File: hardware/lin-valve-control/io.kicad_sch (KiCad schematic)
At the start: 23 parts

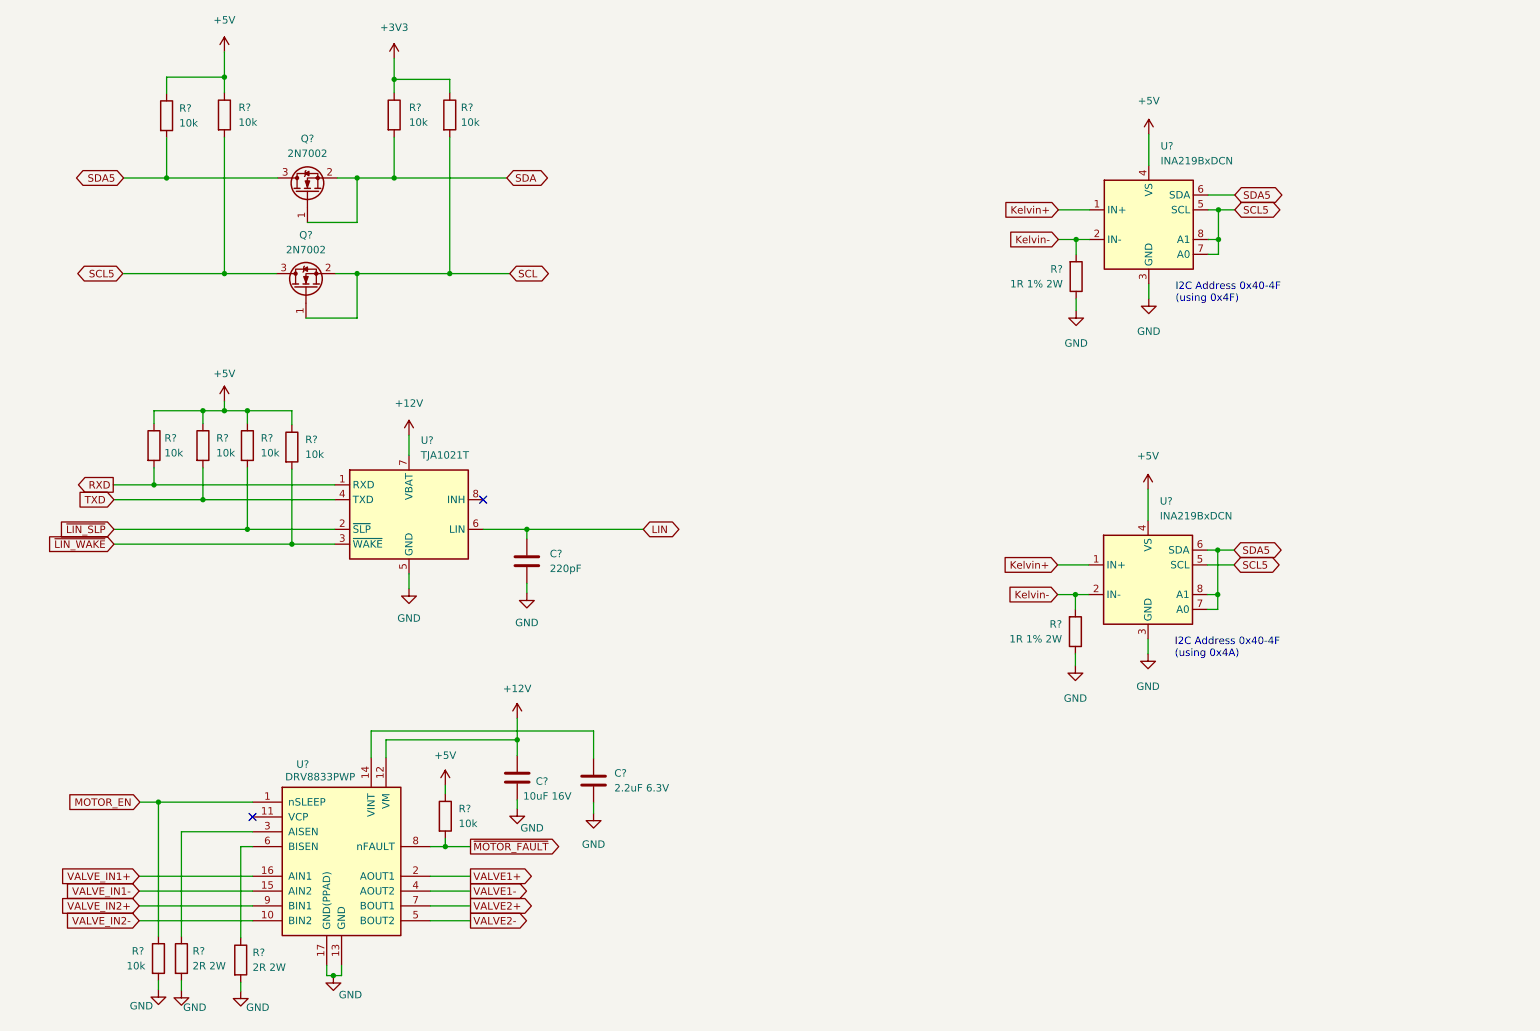
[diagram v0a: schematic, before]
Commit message: Update lin-master firmware and valve control board
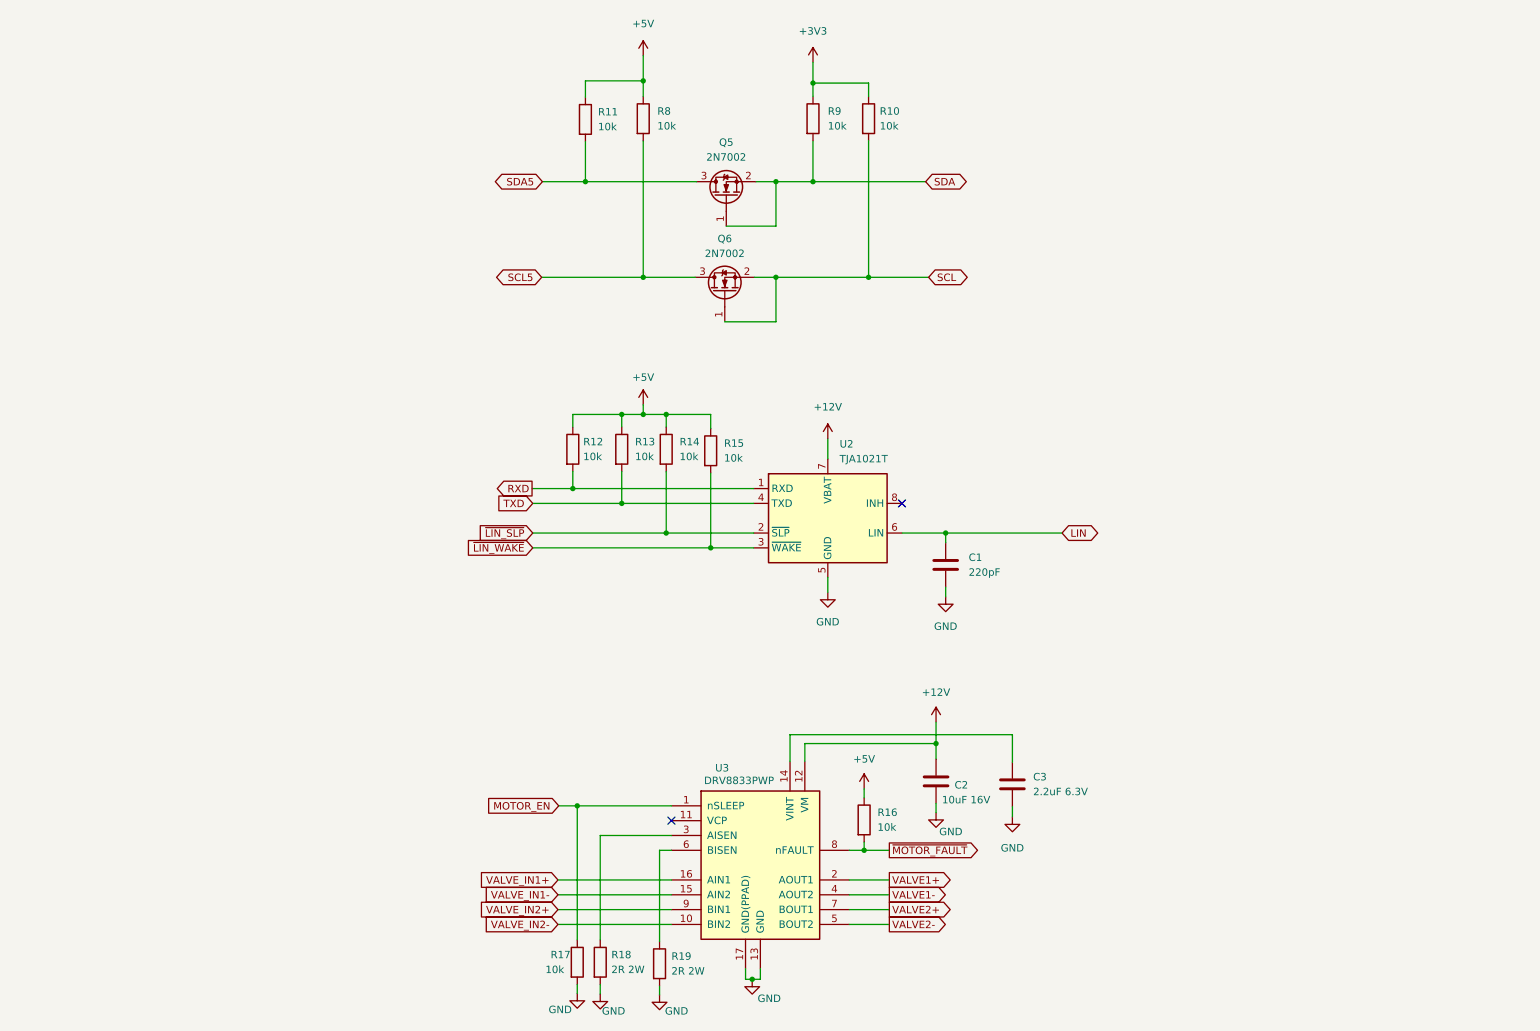
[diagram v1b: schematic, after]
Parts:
- removed R? (x2): 1R 1% 2W, Resistor_SMD:R_2512_6332Metric_Pad1.40x3.35mm_HandSolder, symbol Device:R
- removed U? (x2): INA219BxDCN, Package_TO_SOT_SMD:SOT-23-8, symbol Analog_ADC:INA219BxDCN
- R10, R11, R16, R8, R9: renamed from R?; footprint Resistor_SMD:R_0805_2012Metric -> Resistor_SMD:R_0805_2012Metric_Pad1.20x1.40mm_HandSolder
- gave numbers to parts that had none: 14
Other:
- note removed: "I2C Address 0x40-4F (using 0x4A)"
- note removed: "I2C Address 0x40-4F (using 0x4F)"
- moved on the sheet: C1, C2, C3, Q5, Q6, R10, R11, R12, R13, R14, R15, R16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

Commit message: Updated valve controller board
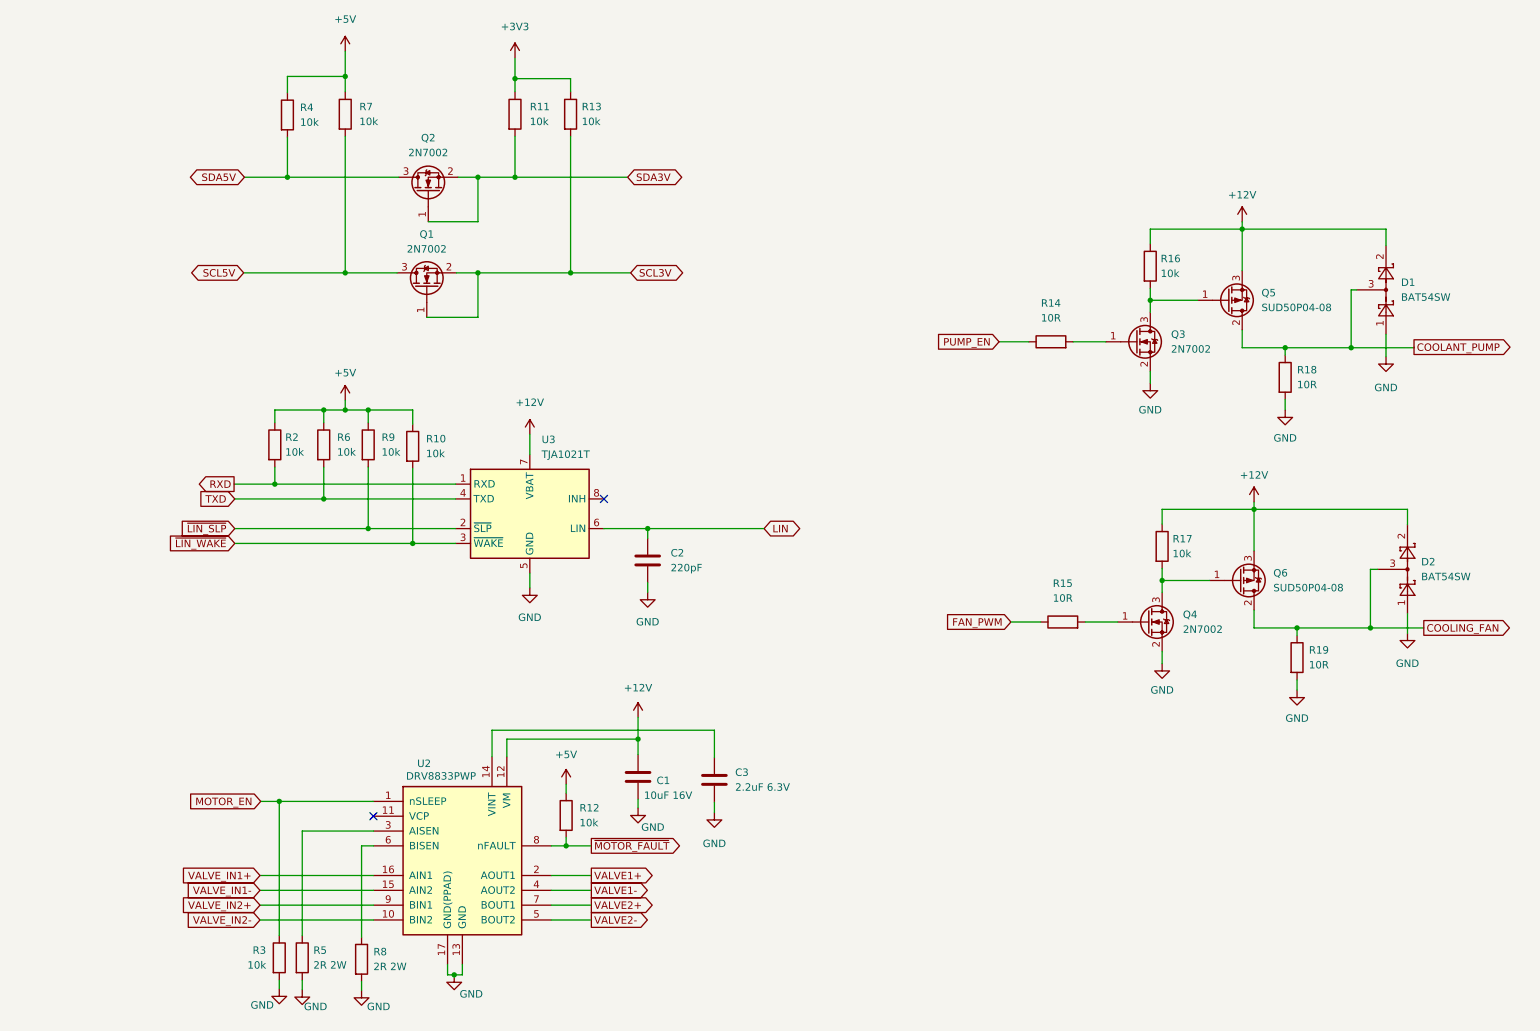
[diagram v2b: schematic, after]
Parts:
- added D1, D2: BAT54SW, Package_TO_SOT_SMD:SOT-323_SC-70, symbol Diode:BAT54SW
- added Q3, Q4: 2N7002, Package_TO_SOT_SMD:SOT-23, symbol Transistor_FET:2N7002
- added Q5, Q6: SUD50P04-08, Package_TO_SOT_SMD:TO-252-2, symbol Transistor_FET:SUD50P04-08
- added R14, R15, R18, R19: 10R, Resistor_SMD:R_0805_2012Metric_Pad1.20x1.40mm_HandSolder, symbol Device:R
- added R16, R17: 10k, Resistor_SMD:R_0805_2012Metric_Pad1.20x1.40mm_HandSolder, symbol Device:R
- renumbered C2 to C1, C1 to C2, Q6 to Q1, Q5 to Q2, R15 to R10, R9 to R11, R16 to R12, R10 to R13, R12 to R2, R17 to R3, R11 to R4, R18 to R5, R13 to R6, R8 to R7, R19 to R8, R14 to R9, U3 to U2, U2 to U3
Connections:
- net +12V: now also D1.2, D2.2, Q5.3 (S), Q6.3 (S), R16.1, R17.1
- net GND: now also D1.1, D2.1, Q3.2 (S), Q4.2 (S), R18.2, R19.2
- net SCL renamed SCL3V
- net SCL5 renamed SCL5V
- net SDA renamed SDA3V
- net SDA5 renamed SDA5V
- new net: Q3.1 (G), R14.2
- new net: Q3.3 (D), Q5.1 (G), R16.2
- new net: Q4.1 (G), R15.2
- new net: Q4.3 (D), Q6.1 (G), R17.2
- new net COOLANT_PUMP: D1.3, Q5.2 (D), R18.1
- new net COOLING_FAN: D2.3, Q6.2 (D), R19.1
- new net FAN_PWM: R15.1
- new net PUMP_EN: R14.1
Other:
- company: (none) -> Gavin Hurlbut
- title: (none) -> LINBus Valve Controller
- moved on the sheet: C1, C2, C3, Q1, Q2, R10, R11, R12, R13, R2, R3, R4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
